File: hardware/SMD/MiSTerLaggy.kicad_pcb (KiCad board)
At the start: 2 copper layers, 10.6 x 15.9 mm, 7 parts, among them J1 USB_C_Receptacle_USB2.0, Q1 PT17-21C/L41/TR8, Q2 2N7002

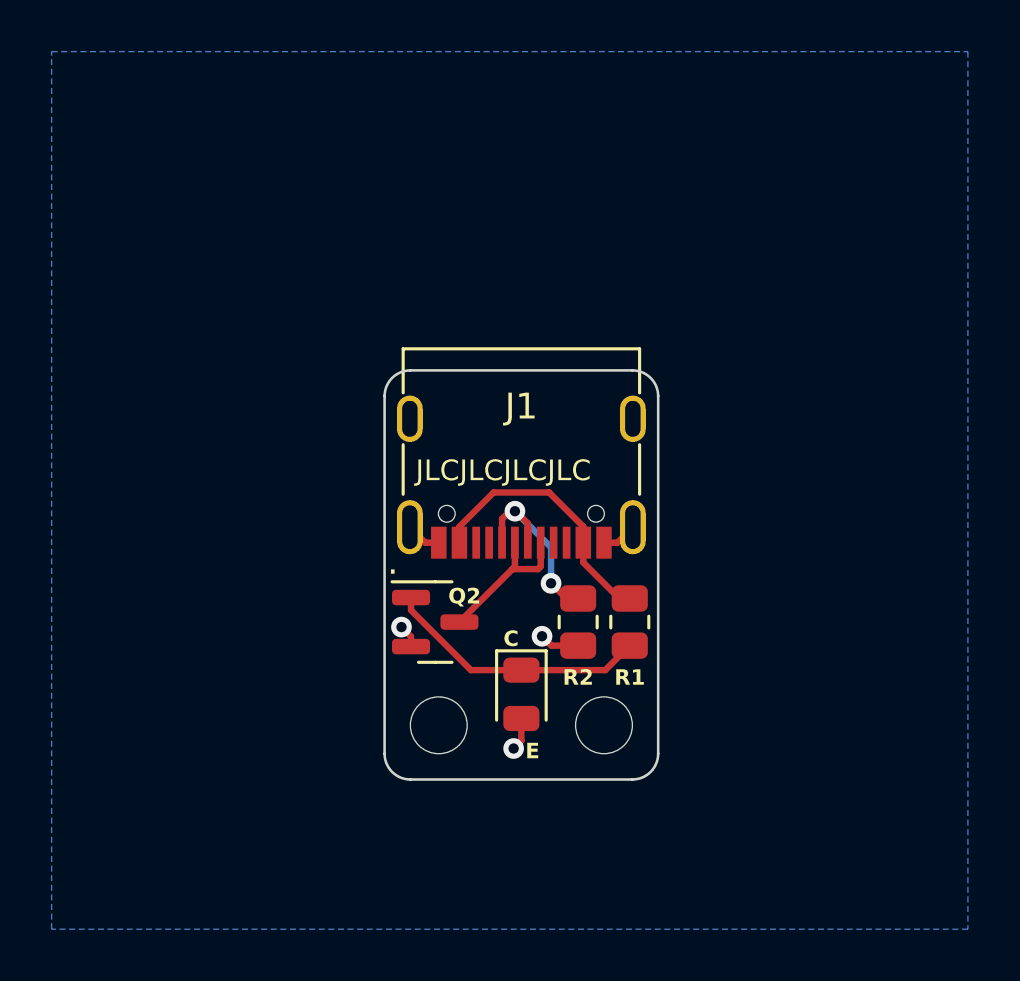
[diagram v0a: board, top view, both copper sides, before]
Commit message: Adjusted layout to make space to isolate the phototransistor
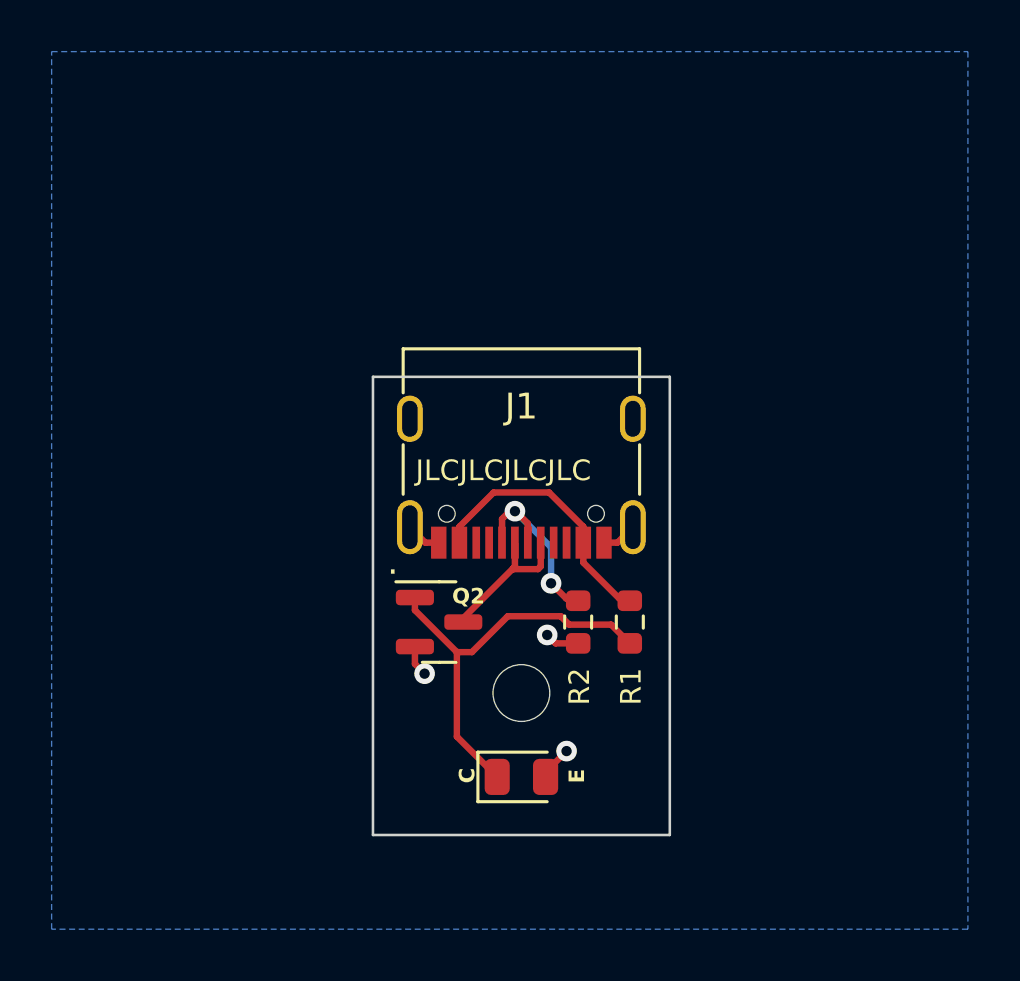
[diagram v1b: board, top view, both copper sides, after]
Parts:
- removed H2: MountingHole_Pad, MountingHole:MountingHole_2.2mm_M2_ISO7380
- R1, R2: footprint Resistor_SMD:R_0805_2012Metric -> Resistor_SMD:R_0603_1608Metric
- moved H1 3.44 mm to (127.7, 81.8)
- moved Q1 3.20 mm to (127.7, 85.1), turned to 0 degrees
- moved Q2 0.15 mm to (124.5, 79.1)
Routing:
- net Net-(Q1-C): track 10.3 -> 16.0 mm
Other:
- board size 10.6 x 15.9 mm -> 11.5 x 17.8 mm

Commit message: Silkscreen changes
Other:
- board text added: "MiSTer Laggy"
- board text removed: "MrLaggy"
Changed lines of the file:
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@@
   (gr_rect (start 121.95 69.6) (end 133.45 87.35)
     (stroke (width 0.1) (type default)) (fill none) (layer "Edge.Cuts"))
-  (gr_text "v1.1" (at 128.65 71 180) (layer "B.SilkS")
+  (gr_text "v1.1" (at 128.65 82.85 180) (layer "B.SilkS")
     (effects (font (size 0.8 0.8) (thickness 0.15)) (justify left bottom mirror))
   )
-  (gr_text "MrLaggy" (at 124.575 72.45 180) (layer "B.SilkS" knockout)
+  (gr_text "MiSTer Laggy" (at 122.7 85.1 180) (layer "B.SilkS" knockout)
     (effects (font (size 1 1) (thickness 0.15)) (justify left bottom mirror))
   )
-  (gr_text "@wickerwaka" (at 124.775 69.9 180) (layer "B.SilkS")
+  (gr_text "@wickerwaka" (at 124.775 72.85 180) (layer "B.SilkS")
     (effects (font (size 0.6 0.6) (thickness 0.1) bold) (justify left bottom mirror))
   )

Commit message: Minor tweaks to silkscreen
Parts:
- R1: value 750K -> 300K
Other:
- board text added: "v1.3"
- board text removed: "v1.1"
